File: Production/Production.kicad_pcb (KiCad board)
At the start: 2 copper layers, 38.5 x 37 mm, 39 parts, among them IC1 MAX3323EEPE+, IC2 AP7375-33SA-7, J1 530480510, J13 FH34SRJ-16S-0.5SH_50_, J2 530480410, J3 USB4085-GF-A_REVB, U2 ADR02AUJZ-REEL7, U3 ATSAMD21G18A-AUT, Y1 32.768, 12.5pF

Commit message: Reloaded footprints & models after switching back to mac
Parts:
- C4: footprint Capacitor_SMD:C_0402_1005Metric -> Capacitor_SMD:C_0805_2012Metric
- J1: footprint Connector_Molex_2:Molex_PicoBlade_53048-0510_1x05_P1.25mm_Horizontal -> Connector_Molex:Molex_PicoBlade_53048-0510_1x05_P1.25mm_Horizontal
- J2: footprint Connector_Molex_2:Molex_PicoBlade_53048-0410_1x04_P1.25mm_Horizontal -> Connector_Molex:Molex_PicoBlade_53048-0410_1x04_P1.25mm_Horizontal
- moved C4 0.51 mm to (101.0, 97.9)
- moved RESET1 0.35 mm to (104.3, 98.4)
- moved C11 0.26 mm to (100.0, 67.2)
- moved R8 0.25 mm to (100.5, 74.0)
- moved D1 0.24 mm to (100.3, 95.8)
- moved C9 0.22 mm to (100.0, 68.3)
- moved C13 0.15 mm to (100.4, 100.0), turned to 180 degrees
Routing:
- net +3V3: track 76.1 -> 78.2 mm
- net SOFTBTN: track 13.7 -> 14.3 mm

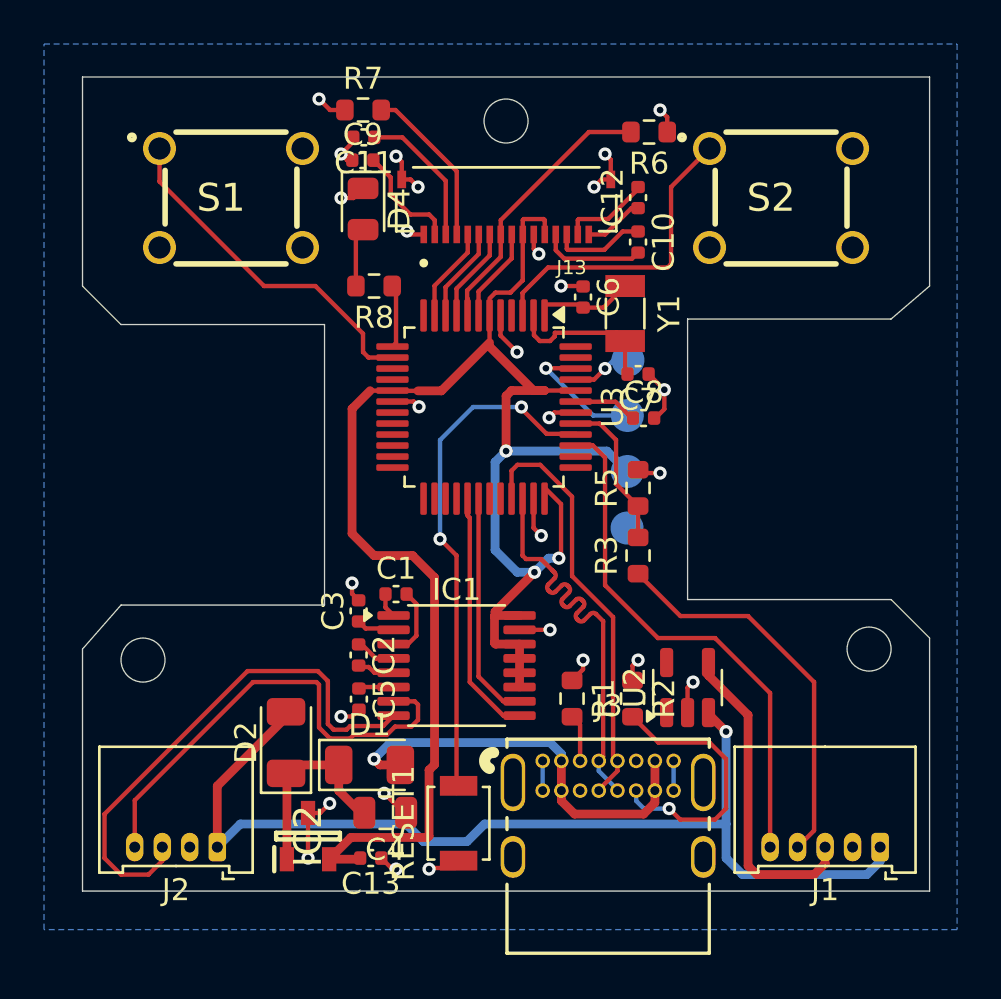
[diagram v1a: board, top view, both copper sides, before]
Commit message: Tweaked some cap sizes & layout accordingly
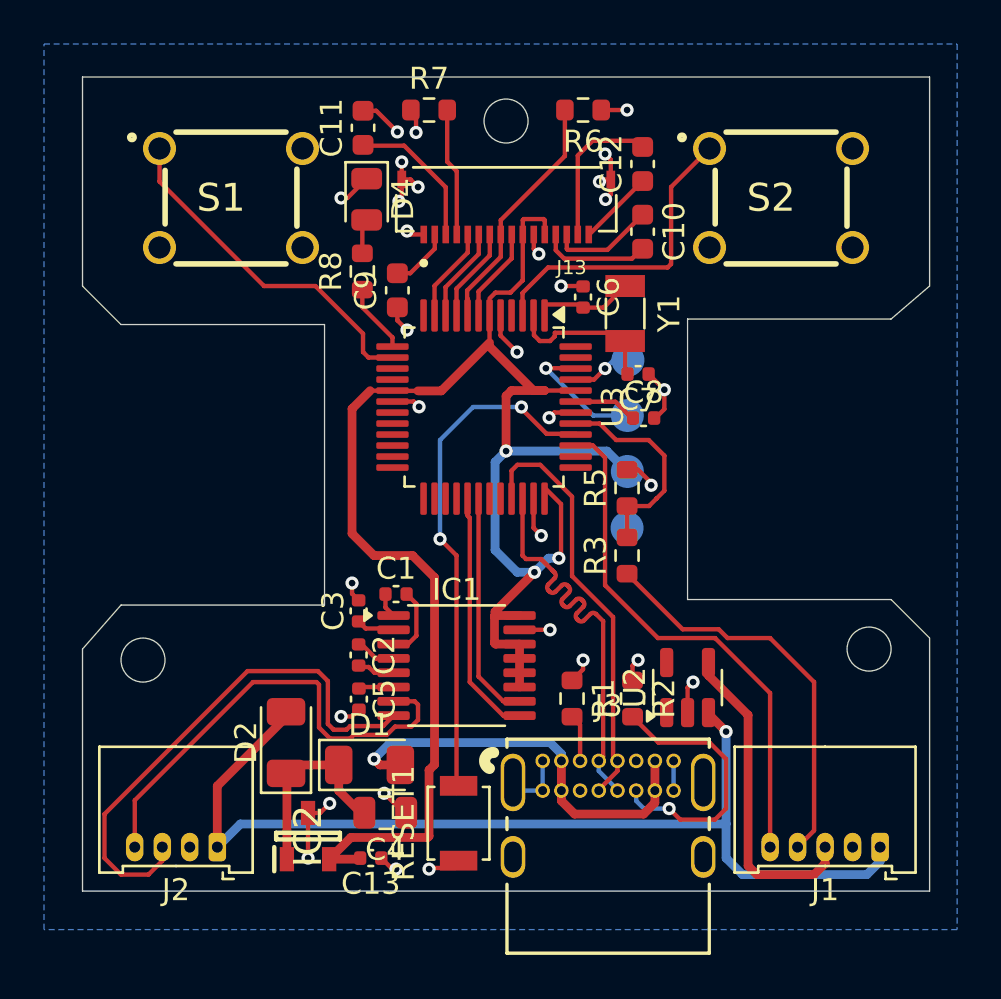
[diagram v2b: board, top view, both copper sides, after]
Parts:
- C10, C11, C12, C9: footprint Capacitor_SMD:C_0402_1005Metric -> Capacitor_SMD:C_0603_1608Metric
- moved C9 6.12 mm to (101.6, 74.2), turned to 90 degrees
- moved R6 3.16 mm to (110.0, 66.0)
- moved R7 3.00 mm to (103.0, 66.0)
- moved C12 1.54 mm to (112.7, 68.5)
- moved R8 0.85 mm to (100.0, 73.3), turned to 90 degrees
- moved C10 0.51 mm to (112.7, 71.5)
- moved R3 0.50 mm to (112.0, 86.2)
- moved R5 0.50 mm to (112.0, 83.2)
- moved D4 0.47 mm to (100.2, 70.1)
- moved C11 0.43 mm to (100.0, 66.8), turned to 90 degrees
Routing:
- net GND: track 38.7 -> 43.7 mm, vias 28 -> 31
- net Net-(C12-Pad2): track 4.07 -> 6.93 mm
- net ZSIG: track 6.99 -> 9.64 mm
- net Net-(C9-Pad2): track 5.03 -> 2.81 mm
- net Net-(J13-Pad4): track 7.46 -> 5.84 mm
- net OLED_RST: track 12.5 -> 11.2 mm
- net Net-(D4-A): track 2.70 -> 1.60 mm
- net Net-(C12-Pad1): track 2.74 -> 3.55 mm
- net +24V: track 46.8 -> 46.2 mm
- net Net-(C10-Pad1): track 4.26 -> 4.78 mm

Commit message: v1, as submitted for production
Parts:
- moved 3V3 10.5 mm to (101.5, 82.6)
- moved GND 10.5 mm to (101.5, 85.2)
- moved SWCLK 10.5 mm to (101.5, 77.5)
- moved SWDIO 10.5 mm to (101.5, 80.0)
- moved R5 3.33 mm to (113.0, 80.0)
- moved R3 3.21 mm to (112.7, 83.1)
- moved C7 2.30 mm to (113.6, 76.0), turned to -90 degrees
- moved C8 1.57 mm to (111.2, 80.1), turned to -90 degrees
- renumbered REF** to 3V3, REF** to GND, REF** to SWCLK, REF** to SWDIO
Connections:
- U3 pad 10: SCK -> unconnected-(U3-PA05-Pad10)
- U3 pad 12: unconnected-(U3-PA07-Pad12) -> SCK
- U3 pad 41: ZSIG -> unconnected-(U3-PA28-Pad41)
- U3 pad 47: unconnected-(U3-PB02-Pad47) -> ZSIG
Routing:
- net SWCLK: track 2.24 -> 10.4 mm
- net GND: track 43.7 -> 49.8 mm, vias 31 -> 33
- net SWDIO: track 5.75 -> 9.74 mm
- net RST: track 23.7 -> 21.4 mm
- net ZSIG: track 9.64 -> 7.42 mm
- net +3V3: track 78.2 -> 76.0 mm, vias 3 -> 4
- net ZOOM: track 18.4 -> 20.2 mm
- net Net-(U3-VDDCORE): track 2.80 -> 1.62 mm
- net SCK: track 4.31 -> 5.38 mm, vias 0 -> 2
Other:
- board text added: "Analog"
- board text added: "MFSerial Production v1 Max Batchelder 2024"
- board text added: "Serial"
- board text added: "Set"
- board text added: "Soft"
